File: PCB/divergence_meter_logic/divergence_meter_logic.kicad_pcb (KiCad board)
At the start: 2 copper layers, 61 parts, among them Q1 BC547, Q10 BC547, Q11 BC547, Q12 BC547, Q13 BC547, Q14 BC547, Q15 BC547, Q16 BC547, Q2 BC547, Q3 BC547, Q4 BC547, Q5 BC547, Q6 BC547, Q7 BC547, Q8 BC547, Q9 BC547

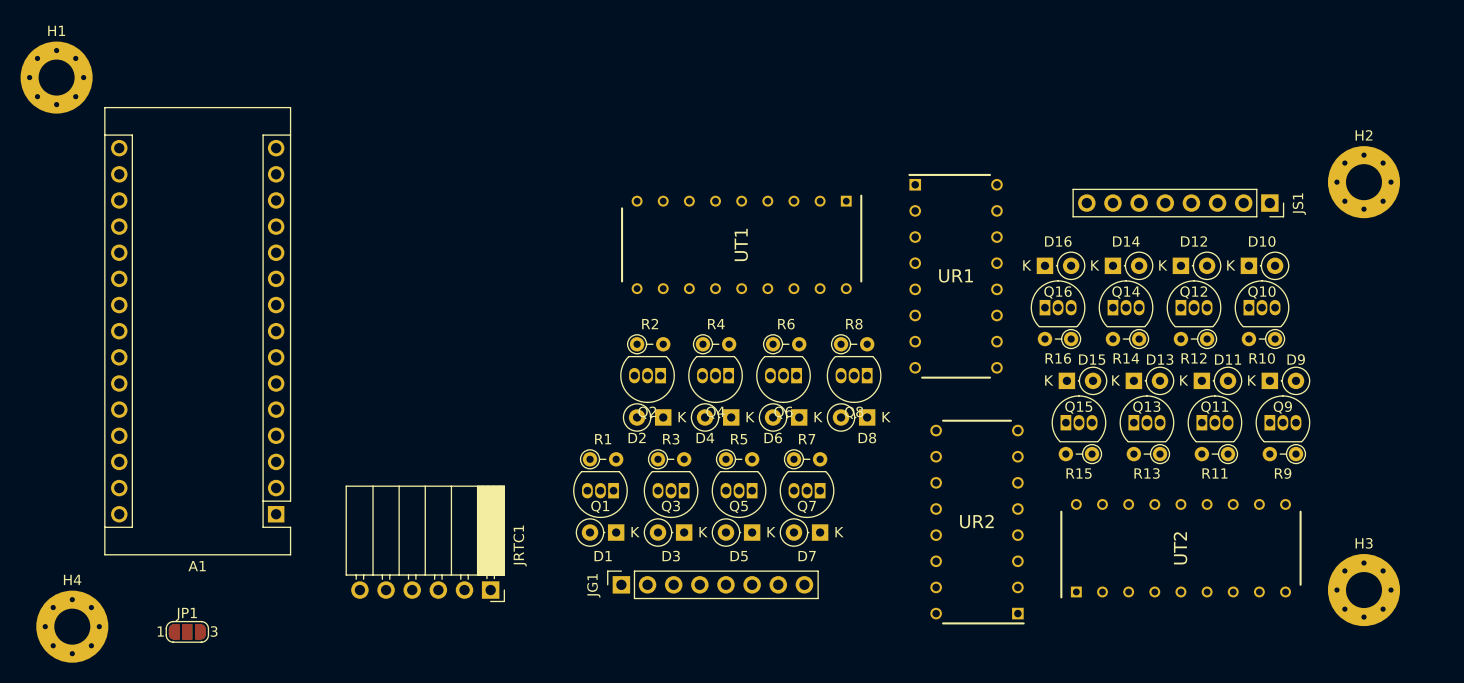
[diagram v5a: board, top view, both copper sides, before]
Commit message: logic pcb almost finished, remaking top
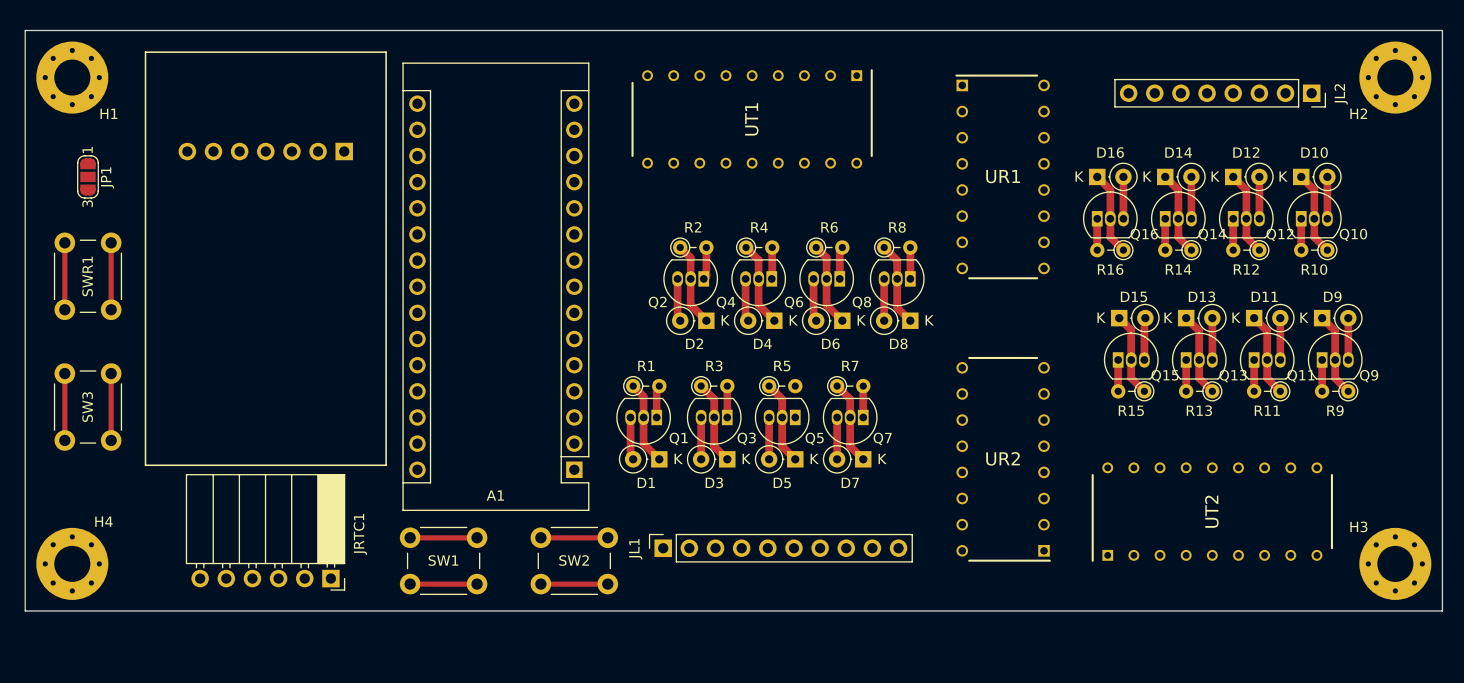
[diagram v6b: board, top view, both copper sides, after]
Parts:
- removed JG1: Conn_01x08, Connector_PinSocket_2.54mm:PinSocket_1x08_P2.54mm_Vertical
- added JL1: Conn_01x10, Connector_PinSocket_2.54mm:PinSocket_1x10_P2.54mm_Vertical, F.Cu at (149.9, 109.2)
- added JPWR1: Conn_01x07, Connector_PinHeader_2.54mm:PinHeader_1x07_P2.54mm_Horizontal, B.Cu at (118.9, 70.7)
- added SW1: SW_Push, Button_Switch_THT:SW_PUSH_6mm_H4.3mm, F.Cu at (125.3, 108.2)
- added SW2: SW_Push, Button_Switch_THT:SW_PUSH_6mm_H4.3mm, F.Cu at (138.0, 108.2)
- added SW3: SW_Push, Button_Switch_THT:SW_PUSH_6mm_H4.3mm, F.Cu at (96.2, 92.3)
- added SWR1: SW_Push, Button_Switch_THT:SW_PUSH_6mm_H4.3mm, F.Cu at (96.2, 79.6)
- moved JP1 45.2 mm to (94.0, 73.2), turned to -90 degrees
- moved A1 29.3 mm to (141.2, 101.6)
- moved JRTC1 15.6 mm to (117.6, 112.2)
- moved UT1 12.2 mm to (158.5, 67.6)
- moved JL2 11.4 mm to (212.9, 65.0)
- moved UR1 10.7 mm to (182.9, 73.2)
- moved H2 10.6 mm to (221.0, 63.5)
- moved D4 10.3 mm to (160.7, 87.1)
- moved D8 10.3 mm to (173.9, 87.1)
- moved Q2 10.3 mm to (153.8, 83.1)
- moved Q4 10.3 mm to (160.4, 83.1)
- moved Q6 10.3 mm to (167.0, 83.1)
- moved Q8 10.3 mm to (173.9, 83.1)
- moved R2 10.3 mm to (151.5, 80.0)
- moved R4 10.3 mm to (157.9, 80.0)
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- renumbered JS1 to JL2
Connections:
- A1 pad 19: Net-(A1-Pad19) -> unconnected-(A1-Pad19)
- A1 pad 20: Net-(A1-Pad20) -> unconnected-(A1-Pad20)
- A1 pad 22: unconnected-(A1-Pad22) -> Net-(SW3-Pad1)
- A1 pad 23: unconnected-(A1-Pad23) -> Net-(A1-Pad23)
- A1 pad 24: unconnected-(A1-Pad24) -> Net-(A1-Pad24)
- A1 pad 25: unconnected-(A1-Pad25) -> Net-(A1-Pad25)
- A1 pad 26: unconnected-(A1-Pad26) -> Net-(A1-Pad26)
- JRTC1 pad 1: GND -> unconnected-(JRTC1-Pad1)
- JRTC1 pad 2: +5V -> unconnected-(JRTC1-Pad2)
- JRTC1 pad 3: Net-(A1-Pad19) -> Net-(A1-Pad24)
- JRTC1 pad 4: Net-(A1-Pad20) -> Net-(A1-Pad23)
- JRTC1 pad 5: unconnected-(JRTC1-Pad5) -> +5V
- JRTC1 pad 6: unconnected-(JRTC1-Pad6) -> GND
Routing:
- net +28V: track 0.00 -> 46.1 mm
- net GND: track 0.00 -> 26.0 mm
- net Net-(D4-Pad1): track 0.00 -> 8.25 mm
- net Net-(D1-Pad1): track 0.00 -> 8.16 mm
- net Net-(D5-Pad1): track 0.00 -> 8.16 mm
- net Net-(D14-Pad1): track 0.00 -> 8.16 mm
- net Net-(D9-Pad1): track 0.00 -> 8.16 mm
- net Net-(D7-Pad1): track 0.00 -> 8.16 mm
- net Net-(D3-Pad1): track 0.00 -> 8.16 mm
- net Net-(D13-Pad1): track 0.00 -> 8.16 mm
- net Net-(D11-Pad1): track 0.00 -> 8.16 mm
- net Net-(D2-Pad1): track 0.00 -> 8.16 mm
- net Net-(D12-Pad1): track 0.00 -> 8.16 mm
- net Net-(D8-Pad1): track 0.00 -> 8.16 mm
- net Net-(D6-Pad1): track 0.00 -> 8.16 mm
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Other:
- board outline added: 137.7 x 56.4 mm
- board text added: "Toohka"

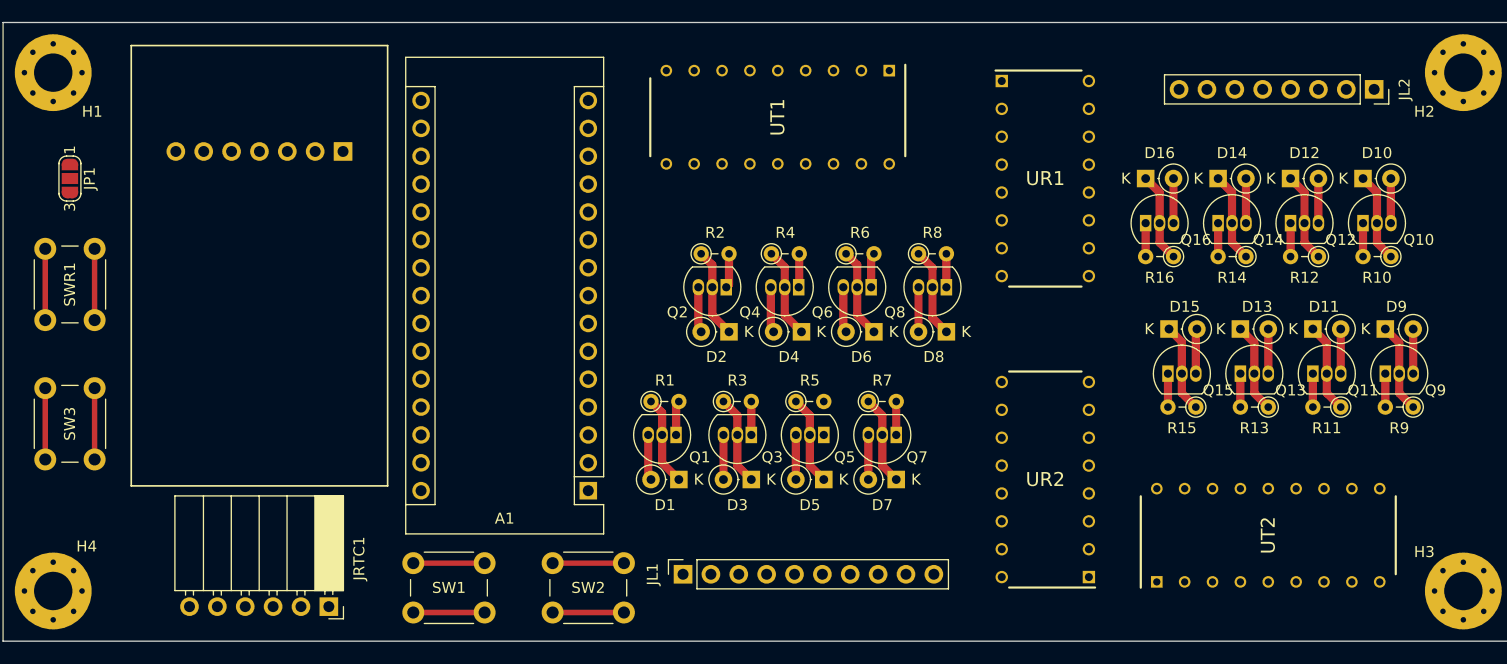
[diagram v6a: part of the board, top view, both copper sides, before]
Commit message: top done, logic almost
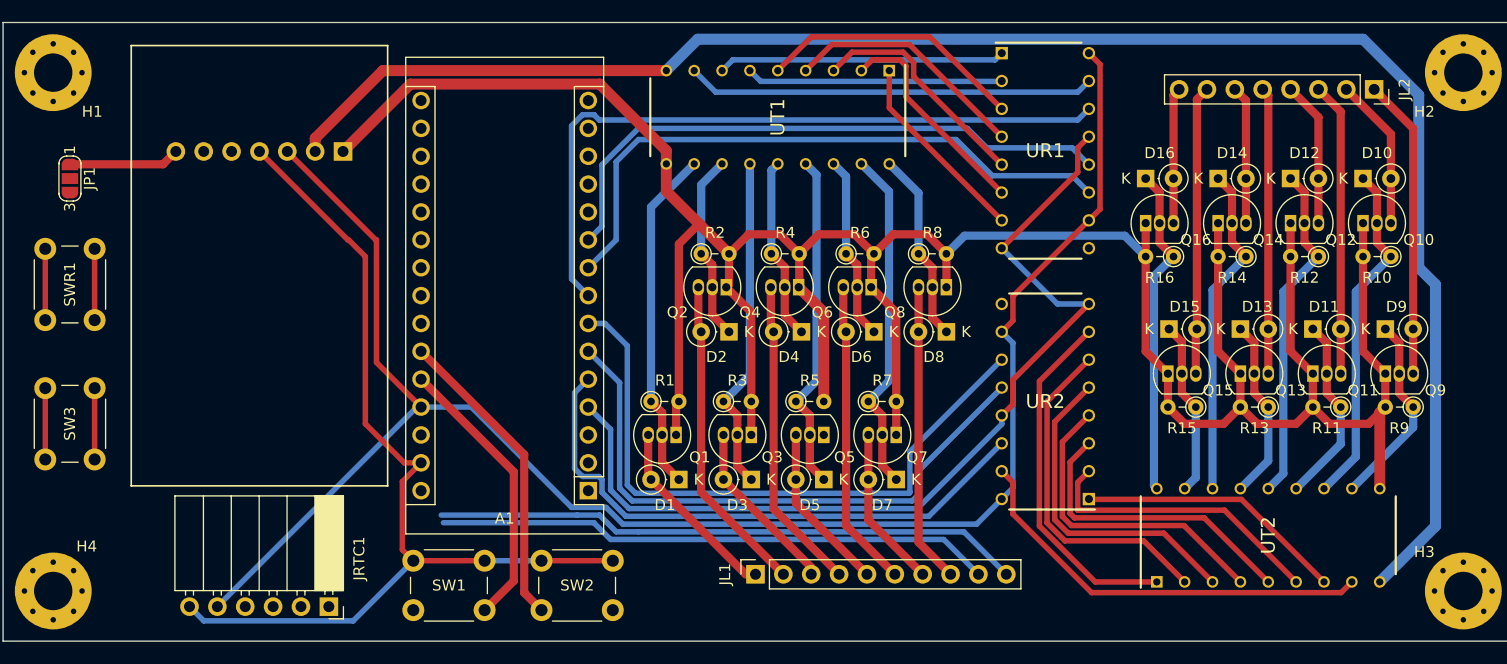
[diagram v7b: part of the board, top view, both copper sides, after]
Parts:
- moved UR2 7.11 mm to (182.9, 93.5)
- moved JL1 6.60 mm to (156.5, 109.2)
- moved UR1 2.54 mm to (182.9, 70.6)
- moved SW2 1.04 mm to (137.0, 108.0)
- moved SW1 0.22 mm to (125.3, 108.0)
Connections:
- A1 pad 10: Net-(A1-Pad10) -> Net-(UR1-Pad12)
- A1 pad 9: Net-(A1-Pad9) -> Net-(UR1-Pad11)
- UR1 pad 11: Net-(A1-Pad10) -> Net-(UR1-Pad11)
- UR1 pad 12: Net-(A1-Pad9) -> Net-(UR1-Pad12)
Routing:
- net +28V: track 46.1 -> 264.5 mm
- net GND: track 26.0 -> 185.5 mm
- net +5V: track 0.00 -> 158.4 mm
- net GND3: track 0.00 -> 154.7 mm
- net Net-(A1-Pad8): track 0.00 -> 64.3 mm
- net Net-(A1-Pad7): track 0.00 -> 58.8 mm
- net Net-(UR1-Pad11): track 0.00 -> 56.6 mm
- net Net-(A1-Pad6): track 0.00 -> 54.5 mm
- net Net-(UR1-Pad12): track 0.00 -> 54.5 mm
- net +1V5: track 0.00 -> 53.7 mm
- net Net-(A1-Pad5): track 0.00 -> 52.8 mm
- net GND1: track 0.00 -> 50.7 mm
- net Net-(UR2-Pad15): track 0.00 -> 38.6 mm
- net Net-(UR1-Pad15): track 0.00 -> 37.2 mm
- net Net-(UR2-Pad7): track 0.00 -> 32.4 mm
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
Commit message: PCB done, exported gerber
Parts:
- moved SW3 12.7 mm to (96.2, 79.6)
- moved SWR1 12.2 mm to (96.2, 91.7)
- moved R10 0.13 mm to (214.4, 80.4)
- moved R12 0.13 mm to (207.8, 80.4)
- moved R14 0.13 mm to (201.2, 80.4)
- moved R16 0.13 mm to (194.6, 80.4)
- moved R2 0.13 mm to (151.5, 79.9)
- moved R4 0.13 mm to (157.9, 79.9)
- moved R6 0.13 mm to (164.7, 79.9)
- moved R8 0.13 mm to (171.3, 79.9)
- moved R1 0.13 mm to (146.9, 93.3)
- moved R11 0.13 mm to (209.8, 94.1)
- moved R13 0.13 mm to (203.2, 94.1)
- moved R15 0.13 mm to (196.6, 94.1)
- moved R3 0.13 mm to (153.5, 93.3)
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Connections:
- net Net-(H1-Pad1) renamed Earth
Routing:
- net GND: track 185.5 -> 249.9 mm
- net GND1: track 50.7 -> 100.4 mm, vias 0 -> 1
- net +1V5: track 53.7 -> 99.0 mm, vias 0 -> 1
- net Net-(A1-Pad23): track 0.00 -> 35.0 mm
- net Net-(A1-Pad24): track 0.00 -> 31.4 mm
- net Net-(A1-Pad28): track 6.50 -> 37.0 mm, vias 0 -> 1
- net Net-(A1-Pad22): track 6.50 -> 37.0 mm
- net +5V: track 158.4 -> 166.0 mm, vias 0 -> 2
- net Net-(A1-Pad25): track 28.1 -> 34.6 mm
- net Net-(A1-Pad26): track 25.6 -> 31.1 mm
- net +28V: track 264.5 -> 266.8 mm
- net Earth: vias 0 -> 11
- added copper zone on B.Cu, net Earth
- added copper zone on F.Cu, net Earth
